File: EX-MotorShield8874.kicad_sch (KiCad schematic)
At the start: 69 parts, among them J101 MC 1,5/ 2-G-3,5, J102 -, J103 MC 1,5/ 2-G-3,5, J104 -, J105 STEMMA QT, J106 Conn_02x04_smd, J107 Conn_01x04_f, Q101 AO3400A, Q102 AO3400A, SW101 Switch, U101 74HC04, U102 74HC08, U103 74HC32, U104 DRV8874PWPR, U105 DRV8874PWPR, U106 LMV321

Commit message: Convert to native KiCad & rework BOM to JLCPCB Basic Parts.
1) Use a KiCad template for an Arduino motor shield as the base.

2) DC-DC Buck converter shows no longer available, select new
   component from JLCPCB's basic list and re-work circuit as necessary.

3) Reworked BOM to use as many JLCPCB basic components as possible.

4) Reworked BOM so all components are in-stock at JLCPCB.

5) Switched to TSSOP for the 74HC logic to save space.e

6) Switched to all KiCad native symbols, which required:
   - Reworking some of the solder jumper logic.
   - Renaming VM to Vdrive.
   - Renaming IOREF to VBUS.
   - Renaming VIN to VCOM.
   - Creating a new symbol library for this project.
   - Creating a new footprint library for this project.
   - Moving a LOT of symbols from _my symbols to KiCad native symbols.

7) Removed unnecessary decoupling capacitors from 74HC logic, a single
   100nF is sufficient.

8) Removed unnecessary decoupling capacitors from Vdrive, not sure why
   they were there.

9) Did a new layout of the board:
   - Started with the DRV8874 chips, layout per data sheet, include
     large multi-layer ground plane to dissipate heat.
   - Moved on to DC-DC buck converter, layout per data sheet, include
     large ground plane to dissipate heat.
   - Put the configuration jumpers in ROUGHLY the same place.
   - Put the I2C OLED and STEMMA connectors in the same place, moved
     the 0.1" pin header connector slightly.

10) Routed everything.

11) Made sure it 100% passed ERC.

12) Made sure it 100% passed DRC.
    - A few exclusions for mechanical holes and silk off the board from the
      template.

13) Uploaded to JLCPCB to price.  Adjusted BOM again due to inventory shortages.
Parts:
- removed A101: Arduino_UNO_R3, _my:Arduino_UNO_R3_edit, symbol MCU_Module:Arduino_UNO_R3
- removed J102, J104: -, _my:PinHeader_01x03_P2.5mm_Vertical_min, symbol Connector_Generic:Conn_01x02
- removed JP101, JP102, JP103, JP105, JP106, JP108, JP109, JP110, JP111, JP112, JP113, JP114, JP115, JP116, JP117: Jumper_3, _my:SolderJumper-3, symbol Jumper:SolderJumper_3_Bridged12
- removed JP104, JP107: Jumper_4, _my:SolderJumper-4, symbol _my:SolderJumper_4
- removed R105, R106: 10k, Resistor_SMD:R_0805_2012Metric_Pad1.20x1.40mm_HandSolder, symbol Device:R_Small
- added C201, C202: 100uF, Capacitor_SMD:CP_Elec_6.3x7.7, symbol Device:C_Polarized_Small
- added D202: EMERALD, LED_SMD:LED_0603_1608Metric, symbol Device:LED
- added J1: Power, Connector_PinSocket_2.54mm:PinSocket_1x08_P2.54mm_Vertical, symbol Connector_Generic:Conn_01x08
- added J2: Digital/PWM, Connector_PinSocket_2.54mm:PinSocket_1x10_P2.54mm_Vertical, symbol Connector_Generic:Conn_01x10
- added J3: Analog, Connector_PinSocket_2.54mm:PinSocket_1x06_P2.54mm_Vertical, symbol Connector_Generic:Conn_01x06
- added J4: Digital/PWM, Connector_PinSocket_2.54mm:PinSocket_1x08_P2.54mm_Vertical, symbol Connector_Generic:Conn_01x08
- added JP11: PWMA, Jumper:SolderJumper-3_P1.3mm_Bridged12_RoundedPad1.0x1.5mm, symbol Jumper:SolderJumper_3_Bridged12
- added JP12: BRKA, Jumper:SolderJumper-3_P1.3mm_Bridged12_RoundedPad1.0x1.5mm, symbol Jumper:SolderJumper_3_Bridged12
- added JP13: PWMB, Jumper:SolderJumper-3_P1.3mm_Bridged12_RoundedPad1.0x1.5mm, symbol Jumper:SolderJumper_3_Bridged12
- added JP14: BRKB, Jumper:SolderJumper-3_P1.3mm_Bridged12_RoundedPad1.0x1.5mm, symbol Jumper:SolderJumper_3_Bridged12
- added JP15: DIRB, Jumper:SolderJumper-3_P1.3mm_Bridged12_RoundedPad1.0x1.5mm, symbol Jumper:SolderJumper_3_Bridged12
- added JP16: DIRA, Jumper:SolderJumper-3_P1.3mm_Bridged12_RoundedPad1.0x1.5mm, symbol Jumper:SolderJumper_3_Bridged12
- added JP17: FLTA, Jumper:SolderJumper-3_P1.3mm_Bridged12_RoundedPad1.0x1.5mm, symbol Jumper:SolderJumper_3_Bridged12
- added JP18: FLTB, Jumper:SolderJumper-3_P1.3mm_Bridged12_RoundedPad1.0x1.5mm, symbol Jumper:SolderJumper_3_Bridged12
- added JP19: SENB, Jumper:SolderJumper-3_P1.3mm_Bridged12_RoundedPad1.0x1.5mm, symbol Jumper:SolderJumper_3_Bridged12
- added JP20: SENA, Jumper:SolderJumper-3_P1.3mm_Bridged12_RoundedPad1.0x1.5mm, symbol Jumper:SolderJumper_3_Bridged12
- added JP23: PMODE, Jumper:SolderJumper-3_P1.3mm_Bridged12_RoundedPad1.0x1.5mm, symbol Jumper:SolderJumper_3_Bridged12
- added JP24: ph/in2a, Jumper:SolderJumper-3_P1.3mm_Bridged12_RoundedPad1.0x1.5mm, symbol Jumper:SolderJumper_3_Bridged12
- added JP25: nSleepb, Jumper:SolderJumper-3_P1.3mm_Bridged12_RoundedPad1.0x1.5mm, symbol Jumper:SolderJumper_3_Bridged12
- added JP26: ph/in2b, Jumper:SolderJumper-3_P1.3mm_Bridged12_RoundedPad1.0x1.5mm, symbol Jumper:SolderJumper_3_Bridged12
- added JP27: nSleepa, Jumper:SolderJumper-3_P1.3mm_Bridged12_RoundedPad1.0x1.5mm, symbol Jumper:SolderJumper_3_Bridged12
- added JP57: B/P A, Jumper:SolderJumper-3_P1.3mm_Bridged12_RoundedPad1.0x1.5mm, symbol Jumper:SolderJumper_3_Bridged12
- added JP58: INA, Jumper:SolderJumper-3_P1.3mm_Bridged12_RoundedPad1.0x1.5mm, symbol Jumper:SolderJumper_3_Bridged12
- added JP59: INB, Jumper:SolderJumper-3_P1.3mm_Bridged12_RoundedPad1.0x1.5mm, symbol Jumper:SolderJumper_3_Bridged12
- added JP60: B/P B, Jumper:SolderJumper-3_P1.3mm_Bridged12_RoundedPad1.0x1.5mm, symbol Jumper:SolderJumper_3_Bridged12
- added R204: 47K, Resistor_SMD:R_0402_1005Metric, symbol Device:R_Small
- C101, C104, C107, C108, C114, C115: value 100n -> 100nF; footprint _my:C_1005_(0402) -> Capacitor_SMD:C_0402_1005Metric; LCSC Part # C1525 -> C307331
- C102, C105: value 10u VM -> 10uF
- C103, C106: value 100n VM -> 100nF; footprint _my:C_1005_(0402) -> Capacitor_SMD:C_0402_1005Metric
- C109, C110: value 22n VM -> 22nF; footprint _my:C_1005_(0402) -> Capacitor_SMD:C_0402_1005Metric; LCSC Part # C337699 -> C1532
- C112, C113: value 22n -> 22nF; footprint _my:C_1005_(0402) -> Capacitor_SMD:C_0402_1005Metric; LCSC Part # C337699 -> C1532
- C215: value 22u -> 22uF
- D203: value 0603_LED_Red -> RED; LCSC Part # C72038 -> C2286
- J101, J103: footprint _my:PhoenixContact_MC_1,5_2-G-3.5_1x02_P3.50mm_Horizontal_edited -> Connector_Phoenix_MC:PhoenixContact_MC_1,5_2-G-3.5_1x02_P3.50mm_Horizontal; rohs_cert_or_in_datasheet n -> y
- J105: rohs_cert_or_in_datasheet obtainable -> y
- J106: value Conn_02x04_smd -> I2C; footprint Connector_PinHeader_2.54mm:PinHeader_2x04_P2.54mm_Vertical_SMD -> Connector_PinHeader_2.54mm:PinHeader_2x04_P2.54mm_Vertical; LCSC Part # C780053 -> (none); rohs_cert_or_in_datasheet n -> (none)
- J107: value Conn_01x04_f -> OLED; footprint _my:PinHeader_1x04_P2.54mm_Vertical_solderpad -> Connector_PinSocket_2.54mm:PinSocket_1x04_P2.54mm_Vertical; LCSC Part # C2935975 -> (none); rohs_cert_or_in_datasheet n -> (none)
- R101, R102, R103, R104, R109, R110, R115, R204: value 47k -> 47K; footprint _my:R_1005_(0402) -> Resistor_SMD:R_0402_1005Metric; LCSC Part # C163440 -> C25792
- R111, R112: value 1k43 -> 1K43; footprint _my:R_1005_(0402) -> Resistor_SMD:R_0402_1005Metric; LCSC Part # C226851 -> C11671
- R113, R114: footprint _my:R_1005_(0402) -> Resistor_SMD:R_0402_1005Metric; LCSC Part # C137939 -> C321605
- R116: value 470k -> 470K; footprint _my:R_1005_(0402) -> Resistor_SMD:R_0402_1005Metric; LCSC Part # C137865 -> C25790
- SW101: value Switch -> RESET; footprint _my:SW_SPST_TS-1088-AR02016 -> DCC-EX-Footprints:TS-1187A; LCSC Part # C720477 -> C318884
- U101: footprint Package_SO:SO-14_3.9x8.65mm_P1.27mm -> Package_SO:TSSOP-14_4.4x5mm_P0.65mm; LCSC Part # C5590 -> C80000
- U102: footprint Package_SO:SO-14_3.9x8.65mm_P1.27mm -> Package_SO:TSSOP-14_4.4x5mm_P0.65mm; LCSC Part # C5593 -> C80001
- U103: footprint Package_SO:SO-14_3.9x8.65mm_P1.27mm -> Package_SO:TSSOP-14_4.4x5mm_P0.65mm; LCSC Part # C5632 -> C282335
- U104, U105: footprint _my:HTSSOP-16-1EP_4.4x5mm_P0.65mm_EP3.4x5mm_Mask2.46_HiAmp -> Package_SO:HTSSOP-16-1EP_4.4x5mm_P0.65mm_EP3.4x5mm_Mask2.46x2.31mm_ThermalVias; symbol _my:DRV8874PWPR -> DCC-EX-Symbols:DRV8874PWPR
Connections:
- net +3V3: now also J1.4 (Pin_4)
- net +5V: now also J1.5 (Pin_5)
- net GND: now also U101.1, U101.11, C201.2, C202.2, D202.1 (K), J1.6 (Pin_6), J1.7 (Pin_7), J2.4 (Pin_4), JP23.3 (B); no longer U101.13, U101.9
- net alt_brake_a: now also J4.1 (Pin_1), JP12.3 (B)
- net alt_brake_b: now also J4.2 (Pin_2), JP14.3 (B)
- net alt_direction_a: now also J2.8 (Pin_8), JP16.3 (B)
- net alt_direction_b: now also J4.4 (Pin_4), JP15.3 (B)
- net alt_fault_n_a: now also J4.8 (Pin_8), JP17.3 (B)
- net alt_fault_n_b: now also J4.7 (Pin_7), JP18.3 (B)
- net alt_pwm_a: now also J4.6 (Pin_6), JP11.3 (B)
- net alt_pwm_b: now also J4.3 (Pin_3), JP13.3 (B)
- net alt_sen_a: now also J3.3 (Pin_3), JP20.3 (B)
- net alt_sen_b: now also J3.4 (Pin_4), JP19.3 (B)
- net brake_a: now also U103.13, JP12.2 (C); no longer U103.12
- net brake_a_n: now also JP57.1 (A)
- net brake_b: now also U101.13, JP14.2 (C); no longer U101.5
- net brake_b_n: now also U101.12, JP60.1 (A); no longer U101.6
- net def_brake_a: now also J2.9 (Pin_9), JP12.1 (A)
- net def_brake_b: now also J2.10 (Pin_10), JP14.1 (A)
- net def_direction_a: now also J2.6 (Pin_6), JP16.1 (A)
- net def_direction_b: now also J2.5 (Pin_5), JP15.1 (A)
- net def_fault_n_a: now also J3.5 (Pin_5), JP17.1 (A)
- net def_fault_n_b: now also J3.6 (Pin_6), JP18.1 (A)
- net def_pwm_a: now also J4.5 (Pin_5), JP11.1 (A)
- net def_pwm_b: now also J2.7 (Pin_7), JP13.1 (A)
- net def_sen_a: now also J3.1 (Pin_1), JP20.1 (A)
- net def_sen_b: now also J3.2 (Pin_2), JP19.1 (A)
- net direction_a: now also U101.5, U103.10, JP16.2 (C), JP24.3 (B); no longer U101.1, U103.13
- net direction_a_n: now also U101.6, U103.12; no longer U101.2, U103.10
- net direction_b: now also U101.9, JP15.2 (C), JP26.3 (B); no longer U101.11
- net direction_b_n: now also U101.8; no longer U101.10
- net en/in1a: now also JP58.1 (A)
- net en/in1b: now also JP59.1 (A)
- net fault_n_a: now also JP17.2 (C)
- net fault_n_b: now also JP18.2 (C)
- net in1_a: now also JP58.2 (C)
- net in1_b: now also JP59.2 (C)
- net in2_a: now also JP24.1 (A)
- net in2_b: now also JP26.1 (A)
- net nSleepa: now also JP27.2 (C)
- net nSleepb: now also JP25.2 (C)
- net or_1a: now also U103.8; no longer U103.11
- net or_2a: now also U103.11; no longer U103.8
- net ph/in2a: now also JP24.2 (C)
- net ph/in2b: now also JP26.2 (C)
- net pmode: now also JP23.2 (C)
- net pwm_a: now also JP11.2 (C), JP27.3 (B), JP57.3 (B)
- net pwm_b: now also JP13.2 (C), JP25.3 (B), JP60.3 (B)
- net reset: now also J1.3 (Pin_3)
- net scl: now also J2.1 (Pin_1)
- net sda: now also J2.2 (Pin_2)
- net sen_a: now also JP20.2 (C)
- net sen_b: now also JP19.2 (C)
- net IOREF renamed VBUS
- net VBUS: now also J1.2 (Pin_2), JP23.1 (A), JP25.1 (A), JP27.1 (A)
- net VM renamed Vdrive
- net Vdrive: now also C201.1, C202.1
- net ioref_is_3V3_not_5V renamed VBUS_is_3V3_not_5V
- net out1a renamed trk1l
- net trk1l: now also D203.1 (K), D203.2 (A); no longer R204.2
- net out1b renamed trk2l
- net trk2l: now also D203.1 (K), D203.2 (A); no longer R204.2
- net out2a renamed trk1r
- net trk1r: now also R204.2; no longer D203.1 (K), D203.2 (A)
- net out2b renamed trk2r
- net trk2r: now also R204.2; no longer D203.1 (K), D203.2 (A)
- new net: JP57.2 (C), JP58.3 (B)
- new net: JP59.3 (B), JP60.2 (C)
- new net: D202.2 (A), R204.1
- new net VCOM: J1.8 (Pin_8), R204.2
- no-connect marks 3 -> 4
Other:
- note added: "* Indicates a PWM-capable pin"
- note added: "Channel A Defaults: D12 - Direction D3 - PWM (work duty) D9 - Brake A0 - current sensing."
- note added: "Channel B Defaults: D13 - Direction D11 - PWM (work duty) D8 - Brake A1 - current sensing"
- note added: "Configuration Logic"
- note added: "DRV8874 (max 6A) Current Sensing: V_prop is limited to VRef inside DRV8874 5V = 0.000455*(1430+732)*A => A=5,08 3,3V = 0.000455* 1430 *A => A=5,07 if subbed with DRV8876 (max 3.5A): 5V = 0.001*(x+y)*A => A= 3,3V = 0.001* x *A => A="
- note added: "DRV8874 Motor Drivers"
- note added: "External Connectivity"
- note added: "Indicators"
- note added: "OpAmp as VBUS Comparator"
- note added: "PH/EN Mode (PMODE Low) nSleep/EN/PH out1/2 0 X X ZZ 1 0 X 00 1 1 0 01 1 1 1 10 nSleep = high / pwm EN = not brake / pwm PH = dir"
- note added: "PWM Mode (PMODE High) nSleep/in1/2 out1/2 O X X ZZ 1 0 0 ZZ 1 0 1 01 1 1 0 10 1 1 1 00 nSleep = high in1 = pwm and ( dir or brake) in2 = pwm and (not dir or brake)"
- note added: "Standard Arduino Headers"
- note added: "candidate values: 2k+1k 3.63/1.65 1% 1k8+(680+220) 4.0/1.83 1% 1k5+(680+100) 4.8/2.2 0.2% 1k43+732(extend.) 5.08 0.1% <-- USED HERE (1k2+120)+680 5.5/2.5 0.0% 1k2+(470+180) 5.9/2.7 2% 1k2+620(extend.) 5.9/2.7 0.1% 1k1+560 (0603) 6.6/3.0 0.4%"
- note removed: "Arduino Header"
- note removed: "DRV8874 (max 6A) Current Sensing: V_prop is limited to VRef inside DRV8874 5V = 0.000455*(1430+732)*A => A=5,08 3,3V = 0.000455* 1430 *A => A=5,07 if subbed with DRV8876 (max 3.5A): 5V = 0.001*(x+y)*A => A= 3,3V = 0.001* x *A => A= --------- candidate values: 2k+1k 3.63/1.65 1% 1k8+(680+220) 4.0/1.83 1% 1k5+(680+100) 4.8/2.2 0.2% 1k43+732(extend.) 5.08 0.1% <-- USED HERE (1k2+120)+680 5.5/2.5 0.0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"
- note removed: "DRV8874 Motor Driver"
- note removed: "DRV8874 control logic: PH/EN Mode (PMODE Low) nSleep/EN/PH out1/2 0 X X ZZ 1 0 X 00 1 1 0 01 1 1 1 10 nSleep = high / pwm EN = not brake / pwm PH = dir PWM Mode (PMODE High) nSleep/in1/2 out1/2 O X X ZZ 1 0 0 ZZ 1 0 1 01 1 1 0 10 1 1 1 00 nSleep = high in1 = pwm and ( dir or brake) in2 = pwm and (not dir or brake)"
- note removed: "Low: EN/PH High: PWM Z: Independent"
- note removed: "OLED Header"
- note removed: "OpAmp as IORef Comparator"
- note removed: "Standard Motorshield Assignments: Channel A: D12 - Direction D3 - PWM (work duty) D9 - Brake A0 - current sensing. Channel B: D13 - Direction D11 - PWM (work duty) D8 - Brake A1 - current sensing"
- note removed: "Track Connector"
- note removed: "Track LEDs"
- note removed: "i2c headers"
- company: semify-eda.com -> (none)
- title: EX-Motorshield8874 -> (none)
- moved on the sheet: C101, C102, C103, C104, C105, C106, C107, C108, C109, C110, C112, C113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

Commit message: Added two pin header parts to the BOM.
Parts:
- J106: LCSC Part # (none) -> C492421
- J107: LCSC Part # (none) -> C2897367
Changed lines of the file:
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@@
       (effects (font (size 1.27 1.27)) hide)
     )
-    (property "Datasheet" "~" (at 133.35 81.28 0)
-      (effects (font (size 1.27 1.27)) hide)
-    )
-    (property "LCSC Part #" "" (at 133.35 81.28 0)
+    (property "Datasheet" "https://datasheet.lcsc.com/lcsc/2306091006_HCTL-PM254-1-04-Z-8-5_C2897367.pdf" (at 133.35 81.28 0)
+      (effects (font (size 1.27 1.27)) hide)
+    )
+    (property "LCSC Part #" "C2897367" (at 133.35 81.28 0)
       (effects (font (size 1.27 1.27)) hide)
     )
@@
       (effects (font (size 1.27 1.27)) hide)
     )
-    (property "Description" "DNP" (at 133.35 81.28 0)
+    (property "Description" "2.54mm Plugin 3A 4P -40℃~+105℃ Straight 1x4P 8.5mm Top Square Holes Plugin,P=2.54mm Female Headers ROHS" (at 133.35 81.28 0)
       (effects (font (size 1.27 1.27)) hide)
     )
@@
       (effects (font (size 1.27 1.27)) hide)
     )
-    (property "Datasheet" "~" (at 132.08 49.53 0)
-      (effects (font (size 1.27 1.27)) hide)
-    )
-    (property "LCSC Part #" "" (at 132.08 49.53 0)
+    (property "Datasheet" "https://datasheet.lcsc.com/lcsc/2003191006_XFCN-PZ254V-12-8P_C492421.pdf" (at 132.08 49.53 0)
+      (effects (font (size 1.27 1.27)) hide)
+    )
+    (property "LCSC Part #" "C492421" (at 132.08 49.53 0)
       (effects (font (size 1.27 1.27)) hide)
     )
@@
       (effects (font (size 1.27 1.27)) hide)
     )
-    (property "Description" "DNP" (at 132.08 49.53 0)
-      (effects (font (size 1.27 1.27)) hide)
-    )
+    (property "Description" "Straight Square Pins 2.5mm 8P 6mm -40℃~+105℃ 3mm 2.54mm 双排 Black Brass 2x4P 2.54mm Plugin,P=2.54mm Pin Headers ROHS" (at 132.08 49.53 0)
+      (effects (font (size 1.27 1.27)) hide)
+    )

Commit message: IOREF detection to MOSFET, new indicator LEDs, reduce capacitor size.
1) Replaced the OpAmp & passives that determined IOREF 3 or 5 with a
   P-Channel MOSFET that does the same thing for less cost, components,
   and board space.

2) Changed indicator LEDs to be RED/GREEN single units.  When on DCC
   they will light RED+GREEN = YELLOW.  When driving a DC load (e.g.
   a motor, or even DC track with PWM) they will light either RED or
   GREEN to indicate direction.  They will also show address 0 stretching
   by changing hue.

3) Reduced the size of several capacitors, updated to more capable parts,
   selecting units that had high stock at LCSC & low cost.

4) Reworked traces to accomodate all of the above and generate some minor
   improvements in trace routing.
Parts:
- removed C114, C115: 100nF, Capacitor_SMD:C_0402_1005Metric, symbol Device:C_Small
- removed D203 (x4): RED, LED_SMD:LED_0603_1608Metric, symbol Device:LED
- removed R116: 470K, Resistor_SMD:R_0402_1005Metric, symbol Device:R_Small
- removed U106: LMV321, Package_TO_SOT_SMD:SOT-23-5, symbol Amplifier_Operational:LM321
- added D54, D55: 18-225A, LED_SMD:LED_LiteOn_LTST-C295K_1.6x0.8mm, symbol Device:LED_Dual_AAKK
- added Q52: LP2301LT1G, Package_TO_SOT_SMD:SOT-23, symbol Transistor_FET:IRF4905
- C102, C105: footprint Capacitor_SMD:C_1206_3216Metric -> Capacitor_SMD:C_0805_2012Metric; LCSC Part # C13585 -> C440198
- C215: LCSC Part # C45783 -> C6119901
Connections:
- net 4V5 is gone; now on net GND: R115.2
- net +5V: now also Q52.3 (S); no longer R115.1
- net VBUS: now also Q52.1 (G); no longer J1.2 (Pin_2)
- net VBUS_is_3V3_not_5V: now also R115.1, Q52.2 (D)
- net trk1l: now also D54.2 (A2), D54.3 (K1)
- net trk2l: now also D55.2 (A2), D55.3 (K1)
- net at R204.1: now also D55.1 (A1), D55.4 (K2)
- net at R204.1: now also D54.1 (A1), D54.4 (K2)
- new net IOREF: J1.2 (Pin_2)
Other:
- note added: "If VBUS (IOREF) is 5V, Vgs = 0V, the PMOS is off, VBUS_is_3V3_not_5V will be pulled down to ground by R11. If VBUS (IOREF) is 3.3V, Vgs = -1.7V, the PMOS is on, VBUS_is_3V3_not_5V will be connected to +5V. Downstream the two NMOS will get a signal of 0, or +5V. A Vgs of +5V will fully turn them on, even though the drain voltage is only 3.3V."
- note added: "LP2301LT1G has Vgs(th) = 0.9V. A BSS84 will likely work, but some have Vgs(th) of 1.7V which leaves no margin."
- note added: "VBUS Voltage Determination"
- note removed: "OpAmp as VBUS Comparator"
- moved on the sheet: R115, R204

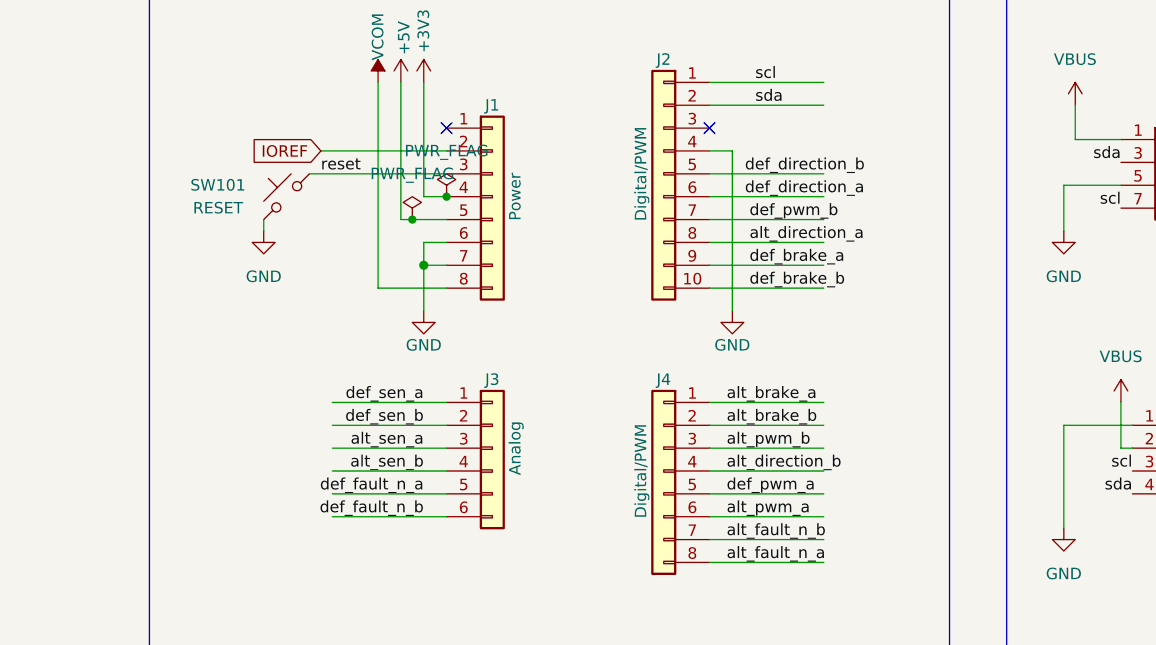
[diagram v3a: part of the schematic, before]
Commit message: Add part numbers for stacking headers.
The stacking headers can be found via global sourcing and hand soldered
by JLCPCB.  Add the part numbers to the BOM.
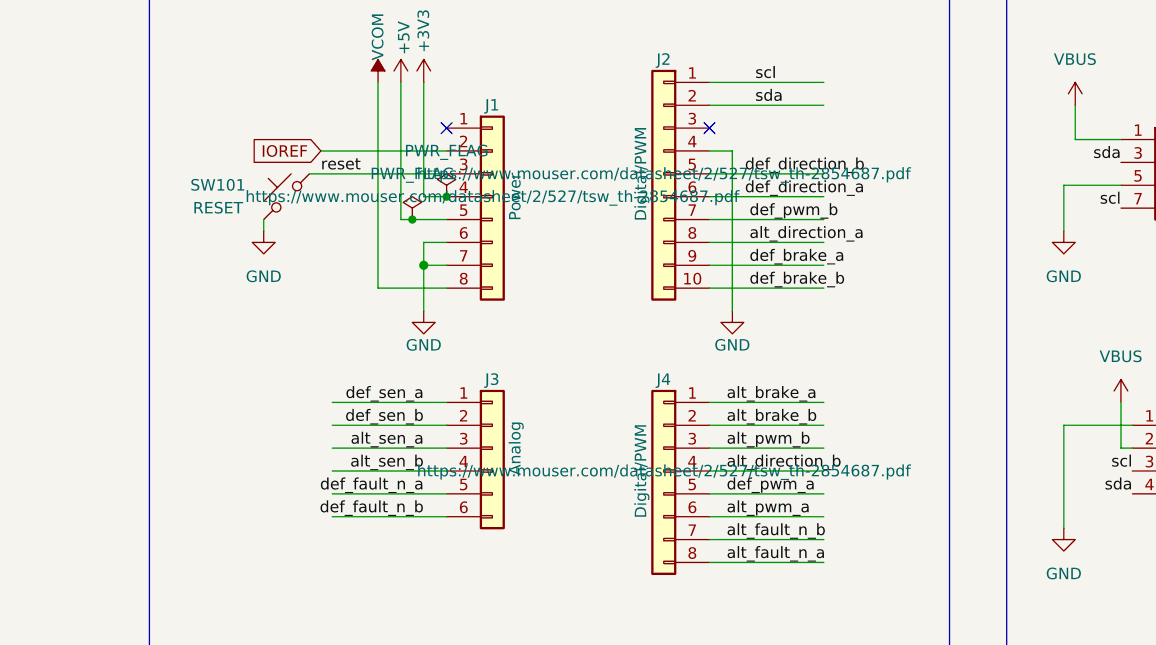
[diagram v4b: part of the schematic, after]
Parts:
- J1, J4: LCSC Part # (none) -> C3330612; rohs_cert_or_in_datasheet (none) -> y
- J106, J107: rohs_cert_or_in_datasheet (none) -> y
- J2: LCSC Part # (none) -> C3334246; rohs_cert_or_in_datasheet (none) -> y
- J3: LCSC Part # (none) -> C3330569; rohs_cert_or_in_datasheet (none) -> y
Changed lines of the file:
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@@
       (effects (font (size 1.27 1.27)) hide)
     )
-    (property "Datasheet" "~" (at 57.15 53.34 0)
+    (property "Datasheet" "https://www.mouser.com/datasheet/2/527/tsw_th-2854687.pdf" (at 57.15 53.34 0)
       (effects (font (size 1.27 1.27)))
     )
-    (property "Description" "DNP" (at 57.15 53.34 0)
+    (property "Description" "Tin Straight Square Pins 2.54mm 8P 5.84mm -55℃~+125℃ 10.16mm 2.54mm Plugin Phosphor bronze Black Plugin,P=2.54mm Pin Headers ROHS" (at 57.15 53.34 0)
+      (effects (font (size 1.27 1.27)) hide)
+    )
+    (property "LCSC Part #" "C3330612" (at 57.15 53.34 0)
+      (effects (font (size 1.27 1.27)) hide)
+    )
+    (property "rohs_cert_or_in_datasheet" "y" (at 57.15 53.34 0)
       (effects (font (size 1.27 1.27)) hide)
     )
@@
       (effects (font (size 1.27 1.27)) hide)
     )
-    (property "Datasheet" "~" (at 76.2 50.8 0)
+    (property "Datasheet" "https://www.mouser.com/datasheet/2/527/tsw_th-2854687.pdf" (at 76.2 50.8 0)
       (effects (font (size 1.27 1.27)))
     )
-    (property "Description" "DNP" (at 76.2 50.8 0)
+    (property "Description" "Tin Straight Square Pins 2.54mm 10P 5.84mm -55℃~+125℃ 10.16mm 2.54mm Plugin Phosphor bronze Black Plugin Pin Headers ROHS" (at 76.2 50.8 0)
+      (effects (font (size 1.27 1.27)) hide)
+    )
+    (property "LCSC Part #" "C3334246" (at 76.2 50.8 0)
+      (effects (font (size 1.27 1.27)) hide)
+    )
+    (property "rohs_cert_or_in_datasheet" "y" (at 76.2 50.8 0)
       (effects (font (size 1.27 1.27)) hide)
     )
@@
       (effects (font (size 1.27 1.27)) hide)
     )
-    (property "Datasheet" "~" (at 57.15 81.28 0)
+    (property "Datasheet" "https://www.mouser.com/datasheet/2/527/tsw_th-2854687.pdf" (at 57.15 81.28 0)
       (effects (font (size 1.27 1.27)) hide)
     )
-    (property "Description" "DNP" (at 57.15 81.28 0)
+    (property "Description" "Tin Straight Square Pins 2.54mm 6P 5.84mm -55℃~+125℃ 10.16mm 2.54mm Plugin Phosphor bronze Black Plugin,P=2.54mm Pin Headers ROHS" (at 57.15 81.28 0)
+      (effects (font (size 1.27 1.27)) hide)
+    )
+    (property "LCSC Part #" "C3330569" (at 57.15 81.28 0)
+      (effects (font (size 1.27 1.27)) hide)
+    )
+    (property "rohs_cert_or_in_datasheet" "y" (at 57.15 81.28 0)
       (effects (font (size 1.27 1.27)) hide)
     )
@@
       (effects (font (size 1.27 1.27)) hide)
     )
-    (property "Datasheet" "~" (at 76.2 83.82 0)
+    (property "Datasheet" "https://www.mouser.com/datasheet/2/527/tsw_th-2854687.pdf" (at 76.2 83.82 0)
       (effects (font (size 1.27 1.27)))
     )
-    (property "Description" "DNP" (at 76.2 83.82 0)
+    (property "Description" "Tin Straight Square Pins 2.54mm 8P 5.84mm -55℃~+125℃ 10.16mm 2.54mm Plugin Phosphor bronze Black Plugin,P=2.54mm Pin Headers ROHS" (at 76.2 83.82 0)
+      (effects (font (size 1.27 1.27)) hide)
+    )
+    (property "LCSC Part #" "C3330612" (at 76.2 83.82 0)
+      (effects (font (size 1.27 1.27)) hide)
+    )
+    (property "rohs_cert_or_in_datasheet" "y" (at 76.2 83.82 0)
       (effects (font (size 1.27 1.27)) hide)
     )
@@
       (effects (font (size 1.27 1.27)) hide)
     )
-    (property "rohs_cert_or_in_datasheet" "" (at 133.35 81.28 0)
+    (property "rohs_cert_or_in_datasheet" "y" (at 133.35 81.28 0)
       (effects (font (size 1.27 1.27)) hide)
     )
@@
       (effects (font (size 1.27 1.27)) hide)
     )
-    (property "rohs_cert_or_in_datasheet" "" (at 132.08 49.53 0)
+    (property "rohs_cert_or_in_datasheet" "y" (at 132.08 49.53 0)
       (effects (font (size 1.27 1.27)) hide)
     )
